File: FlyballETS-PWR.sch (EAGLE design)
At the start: 8 parts

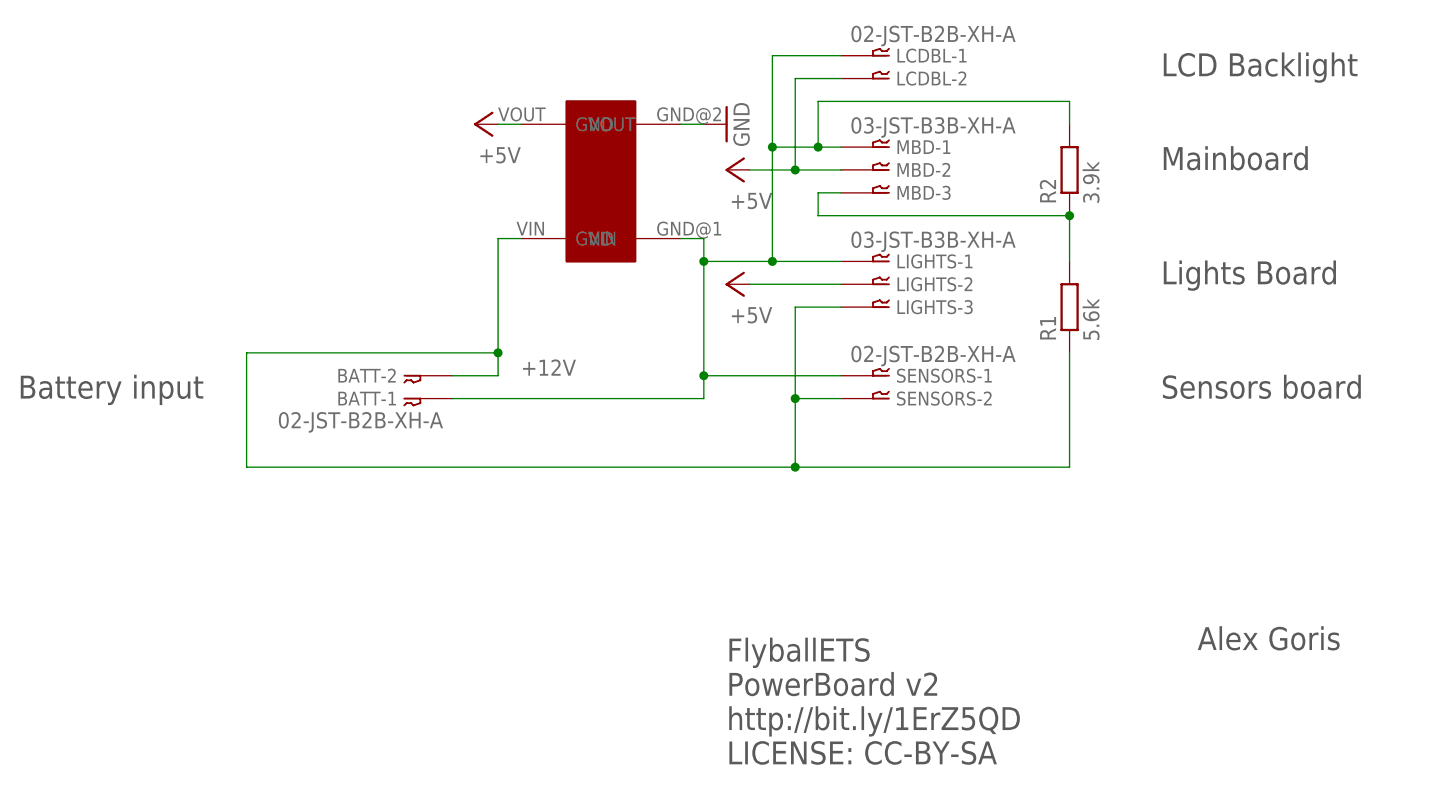
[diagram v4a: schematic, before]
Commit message: Fixed JST XH pin numbering
Updated bt_con-jst-xh.lbr library with swapped pin numbering.
Updated all board designs with updated library so they have the
connectors the right way around
Fixes #4
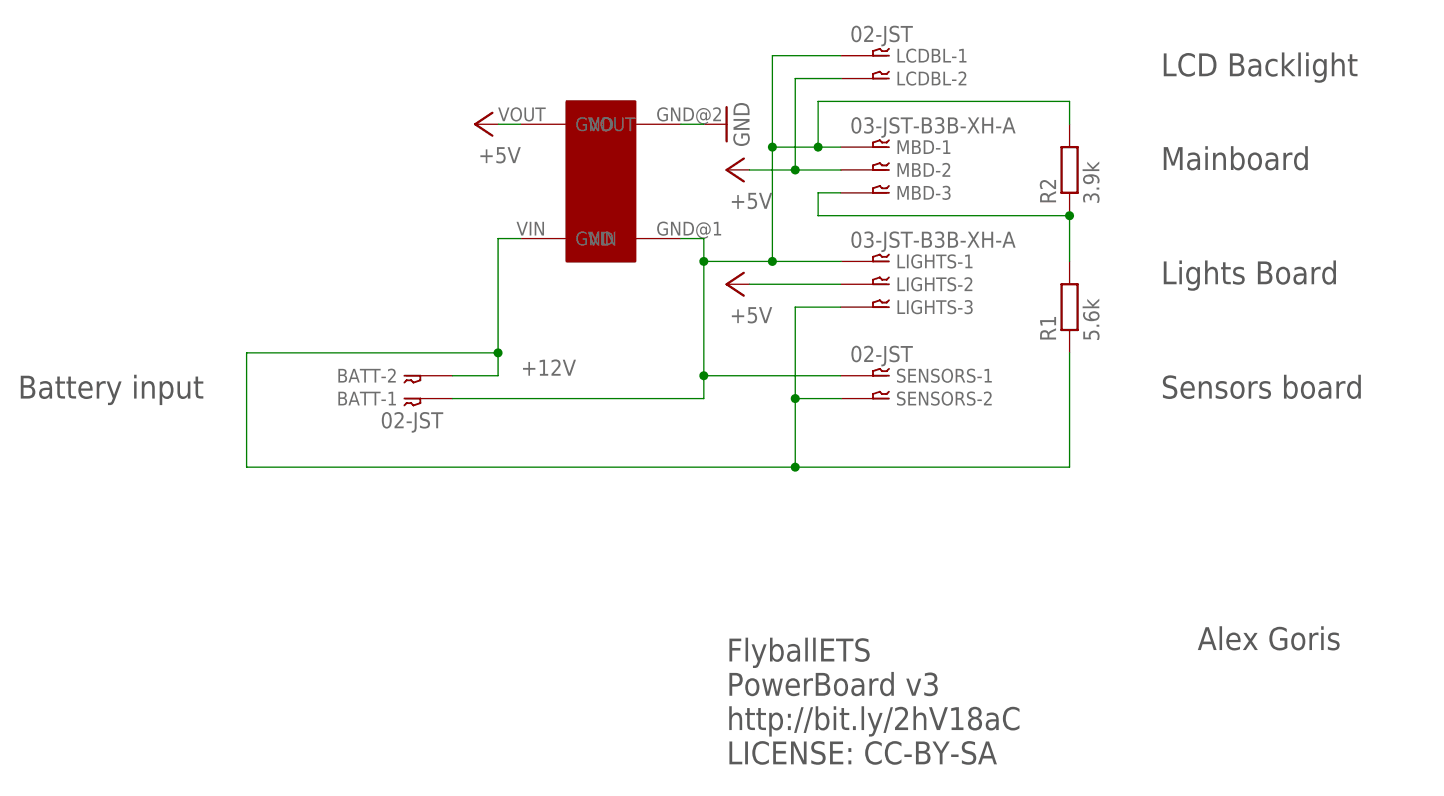
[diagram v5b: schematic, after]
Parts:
- BATT, LCDBL, SENSORS: value 02-JST-B2B-XH-A -> 02-JST; device bt_con-jst-xh:02-JST-B2B-XH-A -> bt_con-jst-xh:02-JST
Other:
- note added: "FlyballETS PowerBoard v3 http://bit.ly/2hV18aC LICENSE: CC-BY-SA"
- note removed: "FlyballETS PowerBoard v2 http://bit.ly/1ErZ5QD LICENSE: CC-BY-SA"
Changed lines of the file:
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@@
 <?xml version="1.0" encoding="utf-8"?>
 <!DOCTYPE eagle SYSTEM "eagle.dtd">
-<eagle version="7.5.0">
+<eagle version="8.2.2">
 <drawing>
 <settings>
@@
 </classes>
 <parts>
-<part name="BATT" library="bt_con-jst-xh" deviceset="02-JST" device="-B2B-XH-A"/>
+<part name="BATT" library="bt_con-jst-xh" deviceset="02-JST" device=""/>
 <part name="MBD" library="bt_con-jst-xh" deviceset="03-JST" device="-B3B-XH-A"/>
-<part name="R1" library="resistor" deviceset="R-EU_" device="0207/10" value="5.6k"/>
-<part name="P+1" library="supply1" deviceset="+5V" device=""/>
-<part name="GND3" library="supply1" deviceset="GND" device=""/>
-<part name="SENSORS" library="bt_con-jst-xh" deviceset="02-JST" device="-B2B-XH-A"/>
+<part name="R1" library="resistor" library_urn="urn:adsk.eagle:library:348" deviceset="R-EU_" device="0207/10" value="5.6k"/>
+<part name="P+1" library="supply1" library_urn="urn:adsk.eagle:library:371" deviceset="+5V" device=""/>
+<part name="GND3" library="supply1" library_urn="urn:adsk.eagle:library:371" deviceset="GND" device=""/>
+<part name="SENSORS" library="bt_con-jst-xh" deviceset="02-JST" device=""/>
 <part name="LIGHTS" library="bt_con-jst-xh" deviceset="03-JST" device="-B3B-XH-A"/>
-<part name="P+3" library="supply1" deviceset="+5V" device=""/>
-<part name="P+5" library="supply1" deviceset="+5V" device=""/>
-<part name="R2" library="resistor" deviceset="R-EU_" device="0207/10" value="3.9k"/>
-<part name="LCDBL" library="bt_con-jst-xh" deviceset="02-JST" device="-B2B-XH-A"/>
+<part name="P+3" library="supply1" library_urn="urn:adsk.eagle:library:371" deviceset="+5V" device=""/>
+<part name="P+5" library="supply1" library_urn="urn:adsk.eagle:library:371" deviceset="+5V" device=""/>
+<part name="R2" library="resistor" library_urn="urn:adsk.eagle:library:348" deviceset="R-EU_" device="0207/10" value="3.9k"/>
+<part name="LCDBL" library="bt_con-jst-xh" deviceset="02-JST" device=""/>
 <part name="U$1" library="_custom" deviceset="LM2596-BOARD" device=""/>
-<part name="FRAME1" library="frames" deviceset="A5L-LOC" device=""/>
+<part name="FRAME1" library="frames" library_urn="urn:adsk.eagle:library:229" deviceset="A5L-LOC" device=""/>
 </parts>
 <sheets>
@@
 <plain>
 <text x="50.8" y="-35.56" size="2.54" layer="97">FlyballETS
-PowerBoard v2
-http://bit.ly/1ErZ5QD
+PowerBoard v3
+http://bit.ly/2hV18aC
 LICENSE: CC-BY-SA</text>
 <text x="103.124" y="-22.86" size="2.54" layer="97">Alex Goris</text>
@@
 which will not be processed correctly with this version.
 </note>
+<note version="8.2" severity="warning">
+Since Version 8.2, Eagle supports online libraries. The ids
+of those online libraries will not be understood (or retained)
+with this version.
+</note>
 </compatibility>
